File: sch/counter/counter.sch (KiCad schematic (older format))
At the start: 25 parts, among them J1 Q1, J10 ~CLK, J11 ~RST, J12 Cout, J13 ~Cout, J14 Vcc, J15 GND, J2 ~Q1, J3 Q2, J4 ~Q2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

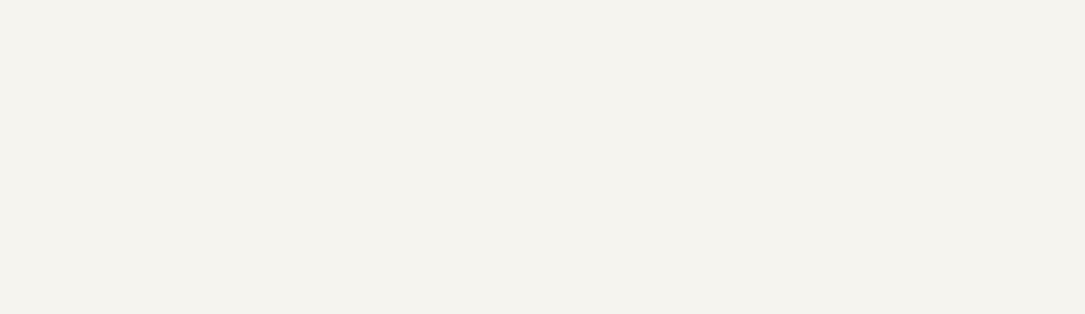
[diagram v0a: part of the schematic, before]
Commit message: One flip-flop is placed on PCB
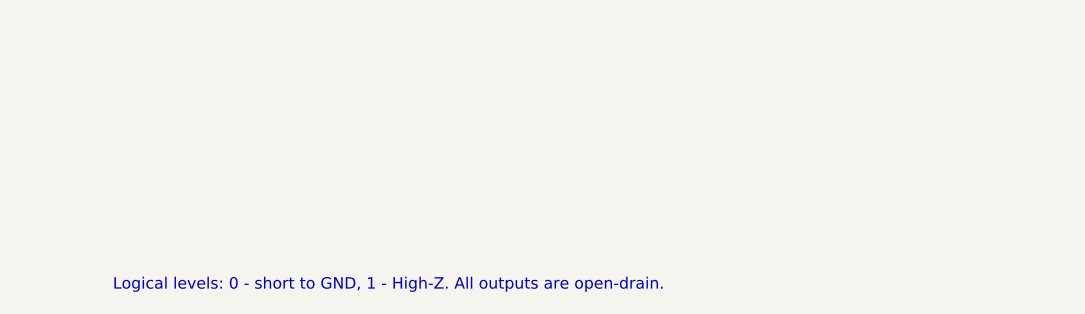
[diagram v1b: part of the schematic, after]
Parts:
- C1: footprint (none) -> Capacitor_SMD:C_0805_2012Metric
- C2: footprint (none) -> Capacitor_Tantalum_SMD:CP_EIA-3528-21_Kemet-B_Pad1.50x2.35mm_HandSolder
- D1, D2, D3, D4: footprint (none) -> LED_SMD:LED_0805_2012Metric_Castellated
- J1, J10, J11, J12, J13, J14, J15, J2, J3, J4, J5, J6, J7, J8, J9: footprint (none) -> Connector_Pin:Pin_D1.0mm_L10.0mm
- R1, R2, R3, R4: footprint (none) -> Resistor_SMD:R_0805_2012Metric
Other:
- note added: "Logical levels: 0 - short to GND, 1 - High-Z. All outputs are open-drain."
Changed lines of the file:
@@
 EESchema Schematic File Version 4
+LIBS:counter-cache
 EELAYER 26 0
 EELAYER END
@@
 F 0 "D1" H 10250 1450 50  0000 C CNN
 F 1 "LED" H 10250 1494 50  0001 C CNN
-F 2 "" V 10250 1350 50  0001 C CNN
+F 2 "LED_SMD:LED_0805_2012Metric_Castellated" V 10250 1350 50  0001 C CNN
 F 3 "~" V 10250 1350 50  0001 C CNN
 	1    10250 1350
@@
 F 0 "R1" V 10293 1350 50  0000 C CNN
 F 1 "330" V 10384 1350 50  0000 C CNN
-F 2 "" V 10430 1350 50  0001 C CNN
+F 2 "Resistor_SMD:R_0805_2012Metric" V 10430 1350 50  0001 C CNN
 F 3 "~" H 10500 1350 50  0001 C CNN
 	1    10500 1350
@@
 $EndComp
 $Comp
-L power:VCC #PWR07
+L power:VCC #PWR06
 U 1 1 5BF76AE1
 P 10650 1350
-F 0 "#PWR07" H 10650 1200 50  0001 C CNN
+F 0 "#PWR06" H 10650 1200 50  0001 C CNN
 F 1 "VCC" H 10667 1523 50  0000 C CNN
 F 2 "" H 10650 1350 50  0001 C CNN
@@
 F 0 "D2" H 10250 1750 50  0000 C CNN
 F 1 "LED" H 10250 1794 50  0001 C CNN
-F 2 "" V 10250 1650 50  0001 C CNN
+F 2 "LED_SMD:LED_0805_2012Metric_Castellated" V 10250 1650 50  0001 C CNN
 F 3 "~" V 10250 1650 50  0001 C CNN
 	1    10250 1650
@@
 F 0 "R2" V 10293 1650 50  0000 C CNN
 F 1 "330" V 10384 1650 50  0000 C CNN
-F 2 "" V 10430 1650 50  0001 C CNN
+F 2 "Resistor_SMD:R_0805_2012Metric" V 10430 1650 50  0001 C CNN
 F 3 "~" H 10500 1650 50  0001 C CNN
 	1    10500 1650
@@
 $EndComp
 $Comp
-L power:VCC #PWR08
+L power:VCC #PWR07
 U 1 1 5BF76B3E
 P 10650 1650
-F 0 "#PWR08" H 10650 1500 50  0001 C CNN
+F 0 "#PWR07" H 10650 1500 50  0001 C CNN
 F 1 "VCC" H 10667 1823 50  0000 C CNN
 F 2 "" H 10650 1650 50  0001 C CNN
@@
 F 0 "D3" H 10250 2050 50  0000 C CNN
 F 1 "LED" H 10250 2094 50  0001 C CNN
-F 2 "" V 10250 1950 50  0001 C CNN
+F 2 "LED_SMD:LED_0805_2012Metric_Castellated" V 10250 1950 50  0001 C CNN
 F 3 "~" V 10250 1950 50  0001 C CNN
 	1    10250 1950
@@
 F 0 "R3" V 10293 1950 50  0000 C CNN
 F 1 "330" V 10384 1950 50  0000 C CNN
-F 2 "" V 10430 1950 50  0001 C CNN
+F 2 "Resistor_SMD:R_0805_2012Metric" V 10430 1950 50  0001 C CNN
 F 3 "~" H 10500 1950 50  0001 C CNN
 	1    10500 1950
@@
 $EndComp
 $Comp
-L power:VCC #PWR09
+L power:VCC #PWR08
 U 1 1 5BF76F0E
 P 10650 1950
-F 0 "#PWR09" H 10650 1800 50  0001 C CNN
+F 0 "#PWR08" H 10650 1800 50  0001 C CNN
 F 1 "VCC" H 10667 2123 50  0000 C CNN
 F 2 "" H 10650 1950 50  0001 C CNN
@@
 F 0 "D4" H 10250 2350 50  0000 C CNN
 F 1 "LED" H 10250 2394 50  0001 C CNN
-F 2 "" V 10250 2250 50  0001 C CNN
+F 2 "LED_SMD:LED_0805_2012Metric_Castellated" V 10250 2250 50  0001 C CNN
 F 3 "~" V 10250 2250 50  0001 C CNN
 	1    10250 2250
@@
 F 0 "R4" V 10293 2250 50  0000 C CNN
 F 1 "330" V 10384 2250 50  0000 C CNN
-F 2 "" V 10430 2250 50  0001 C CNN
+F 2 "Resistor_SMD:R_0805_2012Metric" V 10430 2250 50  0001 C CNN
 F 3 "~" H 10500 2250 50  0001 C CNN
 	1    10500 2250
@@
 $EndComp
 $Comp
-L power:VCC #PWR010
+L power:VCC #PWR09
 U 1 1 5BF772DE
 P 10650 2250
-F 0 "#PWR010" H 10650 2100 50  0001 C CNN
+F 0 "#PWR09" H 10650 2100 50  0001 C CNN
 F 1 "VCC" H 10667 2423 50  0000 C CNN
 F 2 "" H 10650 2250 50  0001 C CNN
@@
 F 0 "J5" H 4400 3550 50  0000 C CNN
 F 1 "Q4" H 4650 3550 50  0000 C CNN
-F 2 "" H 4750 3550 50  0001 C CNN
+F 2 "Connector_Pin:Pin_D1.0mm_L10.0mm" H 4750 3550 50  0001 C CNN
 F 3 "~" H 4750 3550 50  0001 C CNN
 	1    4750 3550
@@
 F 0 "J6" H 4400 3650 50  0000 C CNN
 F 1 "~Q4" H 4650 3650 50  0000 C CNN
-F 2 "" H 4750 3650 50  0001 C CNN
+F 2 "Connector_Pin:Pin_D1.0mm_L10.0mm" H 4750 3650 50  0001 C CNN
 F 3 "~" H 4750 3650 50  0001 C CNN
 	1    4750 3650
@@
 F 0 "J7" H 4400 3750 50  0000 C CNN
 F 1 "Q8" H 4650 3750 50  0000 C CNN
-F 2 "" H 4750 3750 50  0001 C CNN
+F 2 "Connector_Pin:Pin_D1.0mm_L10.0mm" H 4750 3750 50  0001 C CNN
 F 3 "~" H 4750 3750 50  0001 C CNN
 	1    4750 3750
@@
 F 0 "J8" H 4400 3850 50  0000 C CNN
 F 1 "~Q8" H 4650 3850 50  0000 C CNN
-F 2 "" H 4750 3850 50  0001 C CNN
+F 2 "Connector_Pin:Pin_D1.0mm_L10.0mm" H 4750 3850 50  0001 C CNN
 F 3 "~" H 4750 3850 50  0001 C CNN
 	1    4750 3850
@@
 F 0 "J1" H 4400 3150 50  0000 C CNN
 F 1 "Q1" H 4650 3150 50  0000 C CNN
-F 2 "" H 4750 3150 50  0001 C CNN
+F 2 "Connector_Pin:Pin_D1.0mm_L10.0mm" H 4750 3150 50  0001 C CNN
 F 3 "~" H 4750 3150 50  0001 C CNN
 	1    4750 3150
@@
 F 0 "J2" H 4400 3250 50  0000 C CNN
 F 1 "~Q1" H 4650 3250 50  0000 C CNN
-F 2 "" H 4750 3250 50  0001 C CNN
+F 2 "Connector_Pin:Pin_D1.0mm_L10.0mm" H 4750 3250 50  0001 C CNN
 F 3 "~" H 4750 3250 50  0001 C CNN
 	1    4750 3250
@@
 F 0 "J3" H 4400 3350 50  0000 C CNN
 F 1 "Q2" H 4650 3350 50  0000 C CNN
-F 2 "" H 4750 3350 50  0001 C CNN
+F 2 "Connector_Pin:Pin_D1.0mm_L10.0mm" H 4750 3350 50  0001 C CNN
 F 3 "~" H 4750 3350 50  0001 C CNN
 	1    4750 3350
@@
 F 0 "J4" H 4400 3450 50  0000 C CNN
 F 1 "~Q2" H 4650 3450 50  0000 C CNN
-F 2 "" H 4750 3450 50  0001 C CNN
+F 2 "Connector_Pin:Pin_D1.0mm_L10.0mm" H 4750 3450 50  0001 C CNN
 F 3 "~" H 4750 3450 50  0001 C CNN
 	1    4750 3450
@@
 F 0 "J9" H 4400 4050 50  0000 C CNN
 F 1 "CLK" H 4650 4050 50  0000 C CNN
-F 2 "" H 4750 4050 50  0001 C CNN
+F 2 "Connector_Pin:Pin_D1.0mm_L10.0mm" H 4750 4050 50  0001 C CNN
 F 3 "~" H 4750 4050 50  0001 C CNN
 	1    4750 4050
@@
 F 0 "J10" H 4400 4150 50  0000 C CNN
 F 1 "~CLK" H 4650 4150 50  0000 C CNN
-F 2 "" H 4750 4150 50  0001 C CNN
+F 2 "Connector_Pin:Pin_D1.0mm_L10.0mm" H 4750 4150 50  0001 C CNN
 F 3 "~" H 4750 4150 50  0001 C CNN
 	1    4750 4150
@@
 F 0 "J11" H 4400 4350 50  0000 C CNN
 F 1 "~RST" H 4650 4350 50  0000 C CNN
-F 2 "" H 4750 4350 50  0001 C CNN
+F 2 "Connector_Pin:Pin_D1.0mm_L10.0mm" H 4750 4350 50  0001 C CNN
 F 3 "~" H 4750 4350 50  0001 C CNN
 	1    4750 4350
@@
 F 0 "J12" H 4400 4550 50  0000 C CNN
 F 1 "Cout" H 4650 4550 50  0000 C CNN
-F 2 "" H 4750 4550 50  0001 C CNN
+F 2 "Connector_Pin:Pin_D1.0mm_L10.0mm" H 4750 4550 50  0001 C CNN
 F 3 "~" H 4750 4550 50  0001 C CNN
 	1    4750 4550
@@
 F 0 "J13" H 4400 4650 50  0000 C CNN
 F 1 "~Cout" H 4650 4650 50  0000 C CNN
-F 2 "" H 4750 4650 50  0001 C CNN
+F 2 "Connector_Pin:Pin_D1.0mm_L10.0mm" H 4750 4650 50  0001 C CNN
 F 3 "~" H 4750 4650 50  0001 C CNN
 	1    4750 4650
@@
 F 0 "J14" H 4400 4850 50  0000 C CNN
 F 1 "Vcc" H 4650 4850 50  0000 C CNN
-F 2 "" H 4750 4850 50  0001 C CNN
+F 2 "Connector_Pin:Pin_D1.0mm_L10.0mm" H 4750 4850 50  0001 C CNN
 F 3 "~" H 4750 4850 50  0001 C CNN
 	1    4750 4850
@@
 F 0 "J15" H 4400 4950 50  0000 C CNN
 F 1 "GND" H 4650 4950 50  0000 C CNN
-F 2 "" H 4750 4950 50  0001 C CNN
+F 2 "Connector_Pin:Pin_D1.0mm_L10.0mm" H 4750 4950 50  0001 C CNN
 F 3 "~" H 4750 4950 50  0001 C CNN
 	1    4750 4950
@@
 $EndComp
 $Comp
-L power:VCC #PWR04
+L power:VCC #PWR010
 U 1 1 5BF7F2A1
 P 10850 6150
-F 0 "#PWR04" H 10850 6000 50  0001 C CNN
+F 0 "#PWR010" H 10850 6000 50  0001 C CNN
 F 1 "VCC" H 10868 6323 50  0000 C CNN
 F 2 "" H 10850 6150 50  0001 C CNN
@@
 $EndComp
 $Comp
-L power:GND #PWR03
+L power:GND #PWR05
 U 1 1 5BF7F2DA
 P 10450 6150
-F 0 "#PWR03" H 10450 5900 50  0001 C CNN
+F 0 "#PWR05" H 10450 5900 50  0001 C CNN
 F 1 "GND" H 10455 5977 50  0000 C CNN
 F 2 "" H 10450 6150 50  0001 C CNN
@@
 F 0 "C1" H 7915 4596 50  0000 L CNN
 F 1 ".1u" H 7915 4505 50  0000 L CNN
-F 2 "" H 7838 4400 50  0001 C CNN
+F 2 "Capacitor_SMD:C_0805_2012Metric" H 7838 4400 50  0001 C CNN
 F 3 "~" H 7800 4550 50  0001 C CNN
 	1    7800 4550
@@
 F 0 "C2" H 8268 4596 50  0000 L CNN
 F 1 "10u 16v" H 8268 4505 50  0000 L CNN
-F 2 "" H 8188 4400 50  0001 C CNN
+F 2 "Capacitor_Tantalum_SMD:CP_EIA-3528-21_Kemet-B_Pad1.50x2.35mm_HandSolder" H 8188 4400 50  0001 C CNN
 F 3 "~" H 8150 4550 50  0001 C CNN
 	1    8150 4550
@@
 	7800 4400 7950 4400
 $Comp
-L power:VCC #PWR05
+L power:VCC #PWR03
 U 1 1 5BF816CC
 P 7950 4400
-F 0 "#PWR05" H 7950 4250 50  0001 C CNN
+F 0 "#PWR03" H 7950 4250 50  0001 C CNN
 F 1 "VCC" H 7967 4573 50  0000 C CNN
 F 2 "" H 7950 4400 50  0001 C CNN
@@
 	7950 4400 8150 4400
 $Comp
-L power:GND #PWR06
+L power:GND #PWR04
 U 1 1 5BF817EC
 P 8000 4700
-F 0 "#PWR06" H 8000 4450 50  0001 C CNN
+F 0 "#PWR04" H 8000 4450 50  0001 C CNN
 F 1 "GND" H 8005 4527 50  0000 C CNN
 F 2 "" H 8000 4700 50  0001 C CNN
@@
 Wire Wire Line
 	8000 4700 8150 4700
+Text Notes 950  7000 0    50   ~ 0
+Logical levels: 0 - short to GND, 1 - High-Z. All outputs are open-drain.
 $EndSCHEMATC

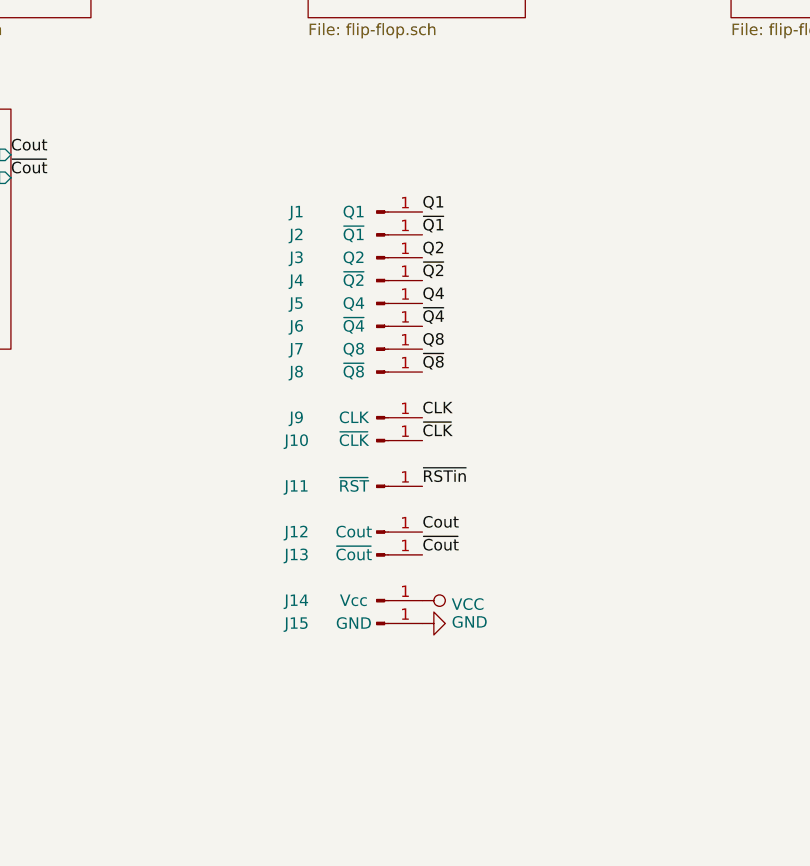
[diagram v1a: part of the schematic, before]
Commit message: Board modified: connectors used
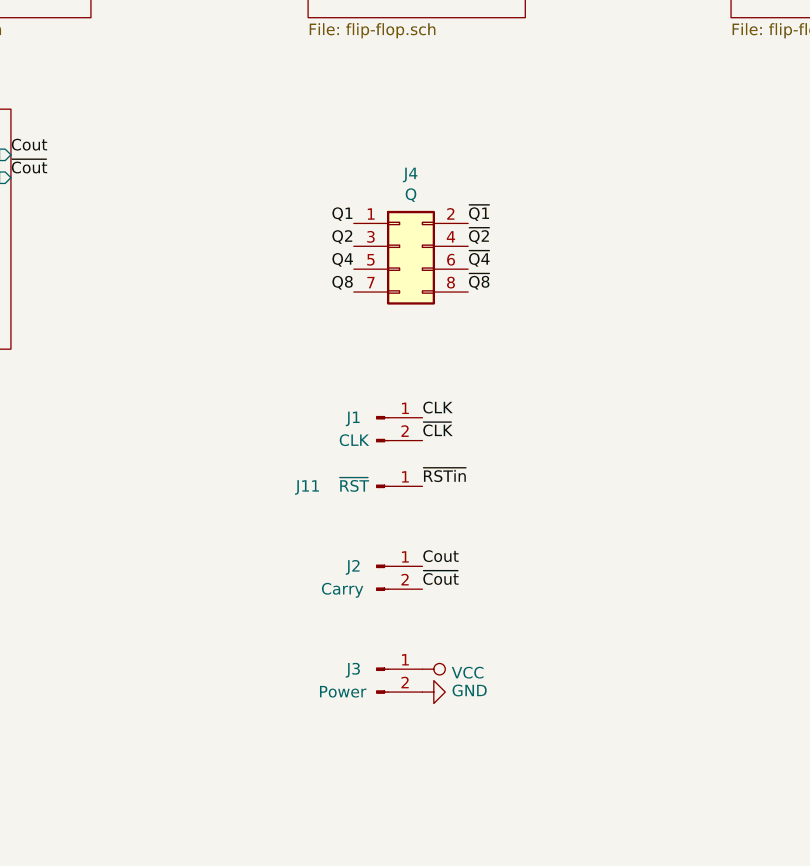
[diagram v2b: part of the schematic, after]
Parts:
- removed J1: Q1, Connector_Pin:Pin_D1.0mm_L10.0mm, symbol Connector:Conn_01x01_Male
- removed J10: ~CLK, Connector_Pin:Pin_D1.0mm_L10.0mm, symbol Connector:Conn_01x01_Male
- removed J12: Cout, Connector_Pin:Pin_D1.0mm_L10.0mm, symbol Connector:Conn_01x01_Male
- removed J13: ~Cout, Connector_Pin:Pin_D1.0mm_L10.0mm, symbol Connector:Conn_01x01_Male
- removed J14: Vcc, Connector_Pin:Pin_D1.0mm_L10.0mm, symbol Connector:Conn_01x01_Male
- removed J15: GND, Connector_Pin:Pin_D1.0mm_L10.0mm, symbol Connector:Conn_01x01_Male
- removed J2: ~Q1, Connector_Pin:Pin_D1.0mm_L10.0mm, symbol Connector:Conn_01x01_Male
- removed J3: Q2, Connector_Pin:Pin_D1.0mm_L10.0mm, symbol Connector:Conn_01x01_Male
- removed J4: ~Q2, Connector_Pin:Pin_D1.0mm_L10.0mm, symbol Connector:Conn_01x01_Male
- removed J5: Q4, Connector_Pin:Pin_D1.0mm_L10.0mm, symbol Connector:Conn_01x01_Male
- removed J6: ~Q4, Connector_Pin:Pin_D1.0mm_L10.0mm, symbol Connector:Conn_01x01_Male
- removed J7: Q8, Connector_Pin:Pin_D1.0mm_L10.0mm, symbol Connector:Conn_01x01_Male
- removed J8: ~Q8, Connector_Pin:Pin_D1.0mm_L10.0mm, symbol Connector:Conn_01x01_Male
- removed J9: CLK, Connector_Pin:Pin_D1.0mm_L10.0mm, symbol Connector:Conn_01x01_Male
- added J1: CLK, Connector_PinHeader_2.54mm:PinHeader_1x02_P2.54mm_Vertical, symbol Connector:Conn_01x02_Male
- added J2: Carry, Connector_PinHeader_2.54mm:PinHeader_1x02_P2.54mm_Vertical, symbol Connector:Conn_01x02_Male
- added J3: Power, Connector_PinHeader_2.54mm:PinHeader_1x02_P2.54mm_Vertical, symbol Connector:Conn_01x02_Male
- added J4: Q, Connector_IDC:IDC-Header_2x04_P2.54mm_Vertical, symbol Connector_Generic:Conn_02x04_Odd_Even
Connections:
- net CLK: now also J1.1 (Pin_1)
- net Cout: now also J2.1 (Pin_1)
- net GND: now also J3.2 (Pin_2)
- net Q1: now also J4.1 (Pin_1)
- net Q2: now also J4.3 (Pin_3)
- net Q4: now also J4.5 (Pin_5)
- net Q8: now also J4.7 (Pin_7)
- net VCC: now also J3.1 (Pin_1)
- net ~CLK: now also J1.2 (Pin_2)
- net ~Cout: now also J2.2 (Pin_2)
- net ~Q1: now also J4.2 (Pin_2)
- net ~Q2: now also J4.4 (Pin_4)
- net ~Q4: now also J4.6 (Pin_6)
- net ~Q8: now also J4.8 (Pin_8)
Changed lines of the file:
@@
 Text Label 3150 3000 0    50   ~ 0
 ~Cout
-$Comp
-L Connector:Conn_01x01_Male J5
-U 1 1 5BF7B786
-P 4750 3550
-F 0 "J5" H 4400 3550 50  0000 C CNN
-F 1 "Q4" H 4650 3550 50  0000 C CNN
-F 2 "Connector_Pin:Pin_D1.0mm_L10.0mm" H 4750 3550 50  0001 C CNN
-F 3 "~" H 4750 3550 50  0001 C CNN
-	1    4750 3550
-	1    0    0    -1
-$EndComp
-$Comp
-L Connector:Conn_01x01_Male J6
-U 1 1 5BF7B88B
-P 4750 3650
-F 0 "J6" H 4400 3650 50  0000 C CNN
-F 1 "~Q4" H 4650 3650 50  0000 C CNN
-F 2 "Connector_Pin:Pin_D1.0mm_L10.0mm" H 4750 3650 50  0001 C CNN
-F 3 "~" H 4750 3650 50  0001 C CNN
-	1    4750 3650
-	1    0    0    -1
-$EndComp
-$Comp
-L Connector:Conn_01x01_Male J7
-U 1 1 5BF7B8AD
-P 4750 3750
-F 0 "J7" H 4400 3750 50  0000 C CNN
-F 1 "Q8" H 4650 3750 50  0000 C CNN
-F 2 "Connector_Pin:Pin_D1.0mm_L10.0mm" H 4750 3750 50  0001 C CNN
-F 3 "~" H 4750 3750 50  0001 C CNN
-	1    4750 3750
-	1    0    0    -1
-$EndComp
-$Comp
-L Connector:Conn_01x01_Male J8
-U 1 1 5BF7B8D1
-P 4750 3850
-F 0 "J8" H 4400 3850 50  0000 C CNN
-F 1 "~Q8" H 4650 3850 50  0000 C CNN
-F 2 "Connector_Pin:Pin_D1.0mm_L10.0mm" H 4750 3850 50  0001 C CNN
-F 3 "~" H 4750 3850 50  0001 C CNN
-	1    4750 3850
-	1    0    0    -1
-$EndComp
-$Comp
-L Connector:Conn_01x01_Male J1
-U 1 1 5BF7BB2C
-P 4750 3150
-F 0 "J1" H 4400 3150 50  0000 C CNN
-F 1 "Q1" H 4650 3150 50  0000 C CNN
-F 2 "Connector_Pin:Pin_D1.0mm_L10.0mm" H 4750 3150 50  0001 C CNN
-F 3 "~" H 4750 3150 50  0001 C CNN
-	1    4750 3150
-	1    0    0    -1
-$EndComp
-$Comp
-L Connector:Conn_01x01_Male J2
-U 1 1 5BF7BB33
-P 4750 3250
-F 0 "J2" H 4400 3250 50  0000 C CNN
-F 1 "~Q1" H 4650 3250 50  0000 C CNN
-F 2 "Connector_Pin:Pin_D1.0mm_L10.0mm" H 4750 3250 50  0001 C CNN
-F 3 "~" H 4750 3250 50  0001 C CNN
-	1    4750 3250
-	1    0    0    -1
-$EndComp
-$Comp
-L Connector:Conn_01x01_Male J3
-U 1 1 5BF7BB3A
-P 4750 3350
-F 0 "J3" H 4400 3350 50  0000 C CNN
-F 1 "Q2" H 4650 3350 50  0000 C CNN
-F 2 "Connector_Pin:Pin_D1.0mm_L10.0mm" H 4750 3350 50  0001 C CNN
-F 3 "~" H 4750 3350 50  0001 C CNN
-	1    4750 3350
-	1    0    0    -1
-$EndComp
-$Comp
-L Connector:Conn_01x01_Male J4
-U 1 1 5BF7BB41
-P 4750 3450
-F 0 "J4" H 4400 3450 50  0000 C CNN
-F 1 "~Q2" H 4650 3450 50  0000 C CNN
-F 2 "Connector_Pin:Pin_D1.0mm_L10.0mm" H 4750 3450 50  0001 C CNN
-F 3 "~" H 4750 3450 50  0001 C CNN
-	1    4750 3450
-	1    0    0    -1
-$EndComp
-Text Label 4950 3150 0    50   ~ 0
-Q1
-Text Label 4950 3250 0    50   ~ 0
-~Q1
-Text Label 4950 3350 0    50   ~ 0
-Q2
-Text Label 4950 3450 0    50   ~ 0
-~Q2
-Text Label 4950 3550 0    50   ~ 0
-Q4
-Text Label 4950 3650 0    50   ~ 0
-~Q4
-Text Label 4950 3750 0    50   ~ 0
-Q8
-Text Label 4950 3850 0    50   ~ 0
-~Q8
-$Comp
-L Connector:Conn_01x01_Male J9
-U 1 1 5BF7CB30
-P 4750 4050
-F 0 "J9" H 4400 4050 50  0000 C CNN
-F 1 "CLK" H 4650 4050 50  0000 C CNN
-F 2 "Connector_Pin:Pin_D1.0mm_L10.0mm" H 4750 4050 50  0001 C CNN
-F 3 "~" H 4750 4050 50  0001 C CNN
-	1    4750 4050
-	1    0    0    -1
-$EndComp
-$Comp
-L Connector:Conn_01x01_Male J10
-U 1 1 5BF7CC44
-P 4750 4150
-F 0 "J10" H 4400 4150 50  0000 C CNN
-F 1 "~CLK" H 4650 4150 50  0000 C CNN
-F 2 "Connector_Pin:Pin_D1.0mm_L10.0mm" H 4750 4150 50  0001 C CNN
-F 3 "~" H 4750 4150 50  0001 C CNN
-	1    4750 4150
-	1    0    0    -1
-$EndComp
 Text Label 4950 4050 0    50   ~ 0
 CLK
@@
 U 1 1 5BF7CFCF
 P 4750 4350
-F 0 "J11" H 4400 4350 50  0000 C CNN
+F 0 "J11" H 4450 4350 50  0000 C CNN
 F 1 "~RST" H 4650 4350 50  0000 C CNN
 F 2 "Connector_Pin:Pin_D1.0mm_L10.0mm" H 4750 4350 50  0001 C CNN
@@
 Text Label 4950 4350 0    50   ~ 0
 ~RSTin
-$Comp
-L Connector:Conn_01x01_Male J12
-U 1 1 5BF7D080
-P 4750 4550
-F 0 "J12" H 4400 4550 50  0000 C CNN
-F 1 "Cout" H 4650 4550 50  0000 C CNN
-F 2 "Connector_Pin:Pin_D1.0mm_L10.0mm" H 4750 4550 50  0001 C CNN
-F 3 "~" H 4750 4550 50  0001 C CNN
-	1    4750 4550
-	1    0    0    -1
-$EndComp
-$Comp
-L Connector:Conn_01x01_Male J13
-U 1 1 5BF7D0E5
-P 4750 4650
-F 0 "J13" H 4400 4650 50  0000 C CNN
-F 1 "~Cout" H 4650 4650 50  0000 C CNN
-F 2 "Connector_Pin:Pin_D1.0mm_L10.0mm" H 4750 4650 50  0001 C CNN
-F 3 "~" H 4750 4650 50  0001 C CNN
-	1    4750 4650
-	1    0    0    -1
-$EndComp
-Text Label 4950 4550 0    50   ~ 0
+Text Label 4950 4700 0    50   ~ 0
 Cout
-Text Label 4950 4650 0    50   ~ 0
+Text Label 4950 4800 0    50   ~ 0
 ~Cout
-$Comp
-L Connector:Conn_01x01_Male J14
-U 1 1 5BF7D641
-P 4750 4850
-F 0 "J14" H 4400 4850 50  0000 C CNN
-F 1 "Vcc" H 4650 4850 50  0000 C CNN
-F 2 "Connector_Pin:Pin_D1.0mm_L10.0mm" H 4750 4850 50  0001 C CNN
-F 3 "~" H 4750 4850 50  0001 C CNN
-	1    4750 4850
-	1    0    0    -1
-$EndComp
-$Comp
-L Connector:Conn_01x01_Male J15
-U 1 1 5BF7D6B0
-P 4750 4950
-F 0 "J15" H 4400 4950 50  0000 C CNN
-F 1 "GND" H 4650 4950 50  0000 C CNN
-F 2 "Connector_Pin:Pin_D1.0mm_L10.0mm" H 4750 4950 50  0001 C CNN
-F 3 "~" H 4750 4950 50  0001 C CNN
-	1    4750 4950
-	1    0    0    -1
-$EndComp
 $Comp
 L power:VCC #PWR01
 U 1 1 5BF7D77B
-P 4950 4850
-F 0 "#PWR01" H 4950 4700 50  0001 C CNN
-F 1 "VCC" V 4967 4978 50  0000 L CNN
-F 2 "" H 4950 4850 50  0001 C CNN
-F 3 "" H 4950 4850 50  0001 C CNN
-	1    4950 4850
+P 4950 5150
+F 0 "#PWR01" H 4950 5000 50  0001 C CNN
+F 1 "VCC" V 4967 5278 50  0000 L CNN
+F 2 "" H 4950 5150 50  0001 C CNN
+F 3 "" H 4950 5150 50  0001 C CNN
+	1    4950 5150
 	0    1    1    0
 $EndComp
@@
 L power:GND #PWR02
 U 1 1 5BF7D85C
-P 4950 4950
-F 0 "#PWR02" H 4950 4700 50  0001 C CNN
-F 1 "GND" V 4955 4822 50  0000 R CNN
-F 2 "" H 4950 4950 50  0001 C CNN
-F 3 "" H 4950 4950 50  0001 C CNN
-	1    4950 4950
+P 4950 5250
+F 0 "#PWR02" H 4950 5000 50  0001 C CNN
+F 1 "GND" V 4955 5122 50  0000 R CNN
+F 2 "" H 4950 5250 50  0001 C CNN
+F 3 "" H 4950 5250 50  0001 C CNN
+	1    4950 5250
 	0    -1   -1   0
 $EndComp
@@
 Text Notes 950  7000 0    50   ~ 0
 Logical levels: 0 - short to GND, 1 - High-Z. All outputs are open-drain.
+$Comp
+L Connector_Generic:Conn_02x04_Odd_Even J4
+U 1 1 5C03C443
+P 4850 3300
+F 0 "J4" H 4900 3617 50  0000 C CNN
+F 1 "Q" H 4900 3526 50  0000 C CNN
+F 2 "Connector_IDC:IDC-Header_2x04_P2.54mm_Vertical" H 4850 3300 50  0001 C CNN
+F 3 "~" H 4850 3300 50  0001 C CNN
+	1    4850 3300
+	1    0    0    -1
+$EndComp
+Text Label 4650 3200 2    50   ~ 0
+Q1
+Text Label 4650 3300 2    50   ~ 0
+Q2
+Text Label 4650 3400 2    50   ~ 0
+Q4
+Text Label 4650 3500 2    50   ~ 0
+Q8
+Text Label 5150 3200 0    50   ~ 0
+~Q1
+Text Label 5150 3300 0    50   ~ 0
+~Q2
+Text Label 5150 3400 0    50   ~ 0
+~Q4
+Text Label 5150 3500 0    50   ~ 0
+~Q8
+$Comp
+L Connector:Conn_01x02_Male J1
+U 1 1 5C03C735
+P 4750 4050
+F 0 "J1" H 4650 4050 50  0000 C CNN
+F 1 "CLK" H 4650 3950 50  0000 C CNN
+F 2 "Connector_PinHeader_2.54mm:PinHeader_1x02_P2.54mm_Vertical" H 4750 4050 50  0001 C CNN
+F 3 "~" H 4750 4050 50  0001 C CNN
+	1    4750 4050
+	1    0    0    -1
+$EndComp
+$Comp
+L Connector:Conn_01x02_Male J2
+U 1 1 5C03C871
+P 4750 4700
+F 0 "J2" H 4650 4700 50  0000 C CNN
+F 1 "Carry" H 4600 4600 50  0000 C CNN
+F 2 "Connector_PinHeader_2.54mm:PinHeader_1x02_P2.54mm_Vertical" H 4750 4700 50  0001 C CNN
+F 3 "~" H 4750 4700 50  0001 C CNN
+	1    4750 4700
+	1    0    0    -1
+$EndComp
+$Comp
+L Connector:Conn_01x02_Male J3
+U 1 1 5C03C971
+P 4750 5150
+F 0 "J3" H 4650 5150 50  0000 C CNN
+F 1 "Power" H 4600 5050 50  0000 C CNN
+F 2 "Connector_PinHeader_2.54mm:PinHeader_1x02_P2.54mm_Vertical" H 4750 5150 50  0001 C CNN
+F 3 "~" H 4750 5150 50  0001 C CNN
+	1    4750 5150
+	1    0    0    -1
+$EndComp
 $EndSCHEMATC
